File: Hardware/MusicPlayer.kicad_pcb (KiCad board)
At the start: 2 copper layers, 100.9 x 86.8 mm, 34 parts, among them J1 USB_B_Micro, J2 AudioJack3, SW1 SW_Nidec_CAS-120A1, SW2 SW_Nidec_CAS-120A1, U1 MICROSD_SPI_OR_SDIO_CARD, U2 AMS1117, U3 ESP32-S3-WROOM-1, U4 TPS61090

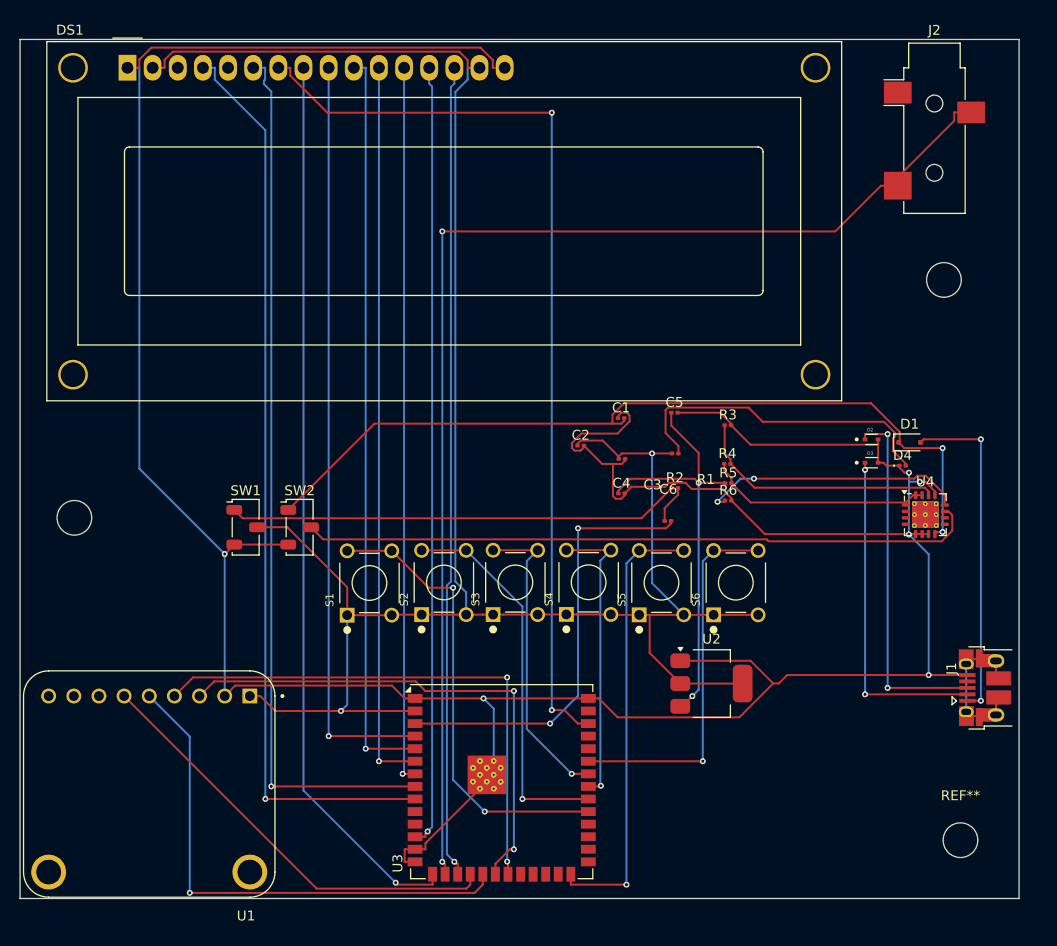
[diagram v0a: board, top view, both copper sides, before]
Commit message: added the button control + volume control
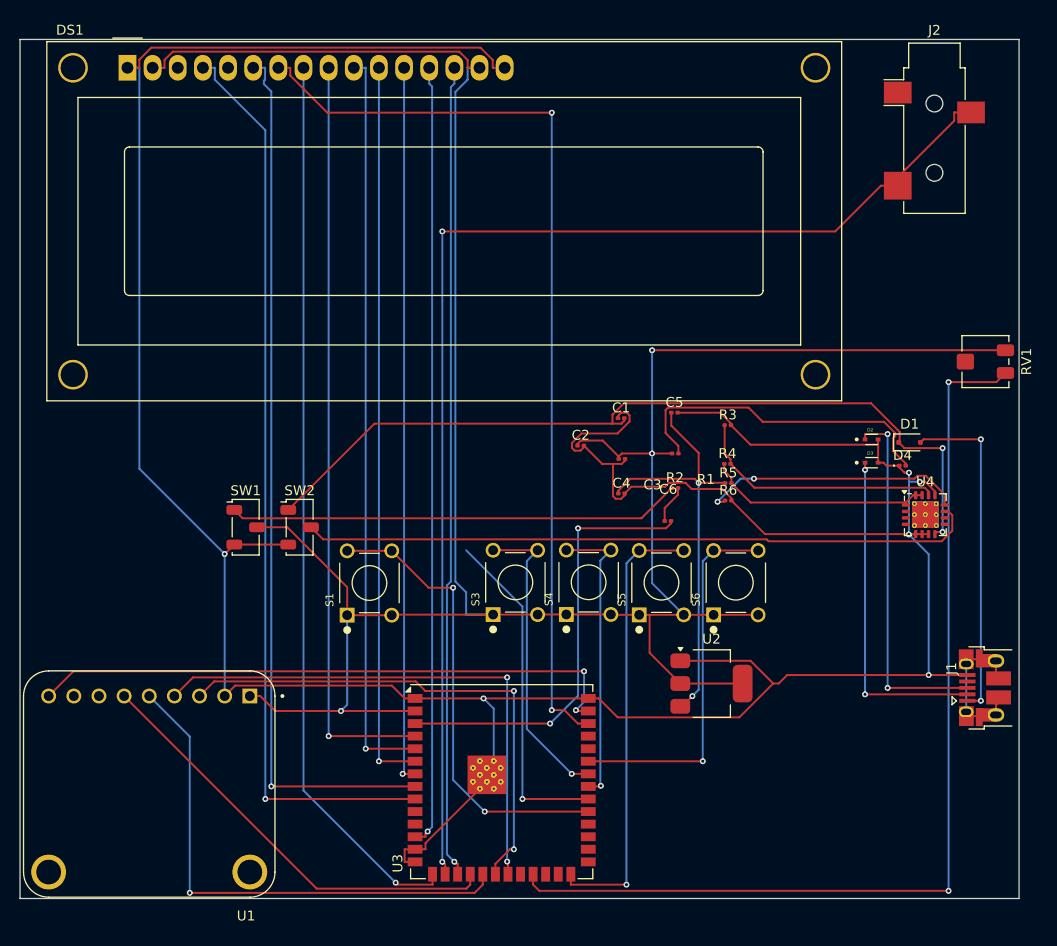
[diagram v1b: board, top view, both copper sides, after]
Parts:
- removed REF** (x3): MountingHole_3.5mm, MountingHole:MountingHole_3.5mm
- removed S2: FSM8JH, FSM8JH:SW_FSM8JH
- added RV1: R_Potentiometer, Potentiometer_SMD:Potentiometer_Bourns_3314S_Horizontal, F.Cu at (97.5, 32.5)
- added U5: ~, 9373129:Untitled, B.Cu at (82.6, 16.3)
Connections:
- U1 pad 9: unconnected-(U1-DET-Pad9) -> SDDET
- U3 pad 23: unconnected-(U3-IO21-Pad23) -> Net-(U3-IO21)
- U3 pad 32: PAUSE -> unconnected-(U3-IO39-Pad32)
- U3 pad 39: unconnected-(U3-IO1-Pad39) -> SDDET
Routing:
- net Net-(U3-IO21): track 0.00 -> 100.8 mm, vias 0 -> 2
- net SDDET: track 0.00 -> 60.7 mm, vias 0 -> 2
- net VCC_3V3: track 219.0 -> 267.8 mm, vias 2 -> 3
- net PAUSE: track 38.6 -> 0.00 mm, vias 1 -> 0
- net unconnected-(U3-IO39-Pad32): track 0.00 -> 34.1 mm, vias 0 -> 1

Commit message: temporarily removed DAC, i think i will change the MCU to one with a built in DAC
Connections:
- J2 pad R: Net-(U3-IO46) -> Net-(J2-PadR)
- J2 pad T: Net-(U3-IO46) -> Net-(J2-PadR)
- U3 pad 16: Net-(U3-IO46) -> unconnected-(U3-IO46-Pad16)
- U3 pad 30: unconnected-(U3-IO37-Pad30) -> SDDET
- U3 pad 39: SDDET -> unconnected-(U3-IO1-Pad39)
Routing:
- net Net-(U3-IO46): track 124.8 -> 0.00 mm, vias 2 -> 0
- net Net-(J2-PadR): track 0.00 -> 78.7 mm, vias 0 -> 2
- net unconnected-(U3-IO17-Pad10): track 0.00 -> 54.7 mm, vias 0 -> 2
- net unconnected-(U3-IO18-Pad11): track 0.00 -> 48.3 mm, vias 0 -> 2
- net VCC_3V3: track 267.8 -> 290.6 mm, vias 3 -> 4
- net SDDET: track 60.7 -> 78.9 mm, vias 2 -> 3
- net D+: track 346.6 -> 359.9 mm
